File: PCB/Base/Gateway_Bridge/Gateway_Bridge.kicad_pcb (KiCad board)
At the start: 2 copper layers, 98.9 x 70.1 mm, 58 parts, among them J1 J_DIAG, J2 J_I2C2, J3 STM32_Breakout, J5 J_CAN_TERM, J6 J_I2C1, J7 J_SWD, J8 J_BUS_IN, J9 J_BUS_OUT, SW1 RESET, U1 STM32F103C8Tx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

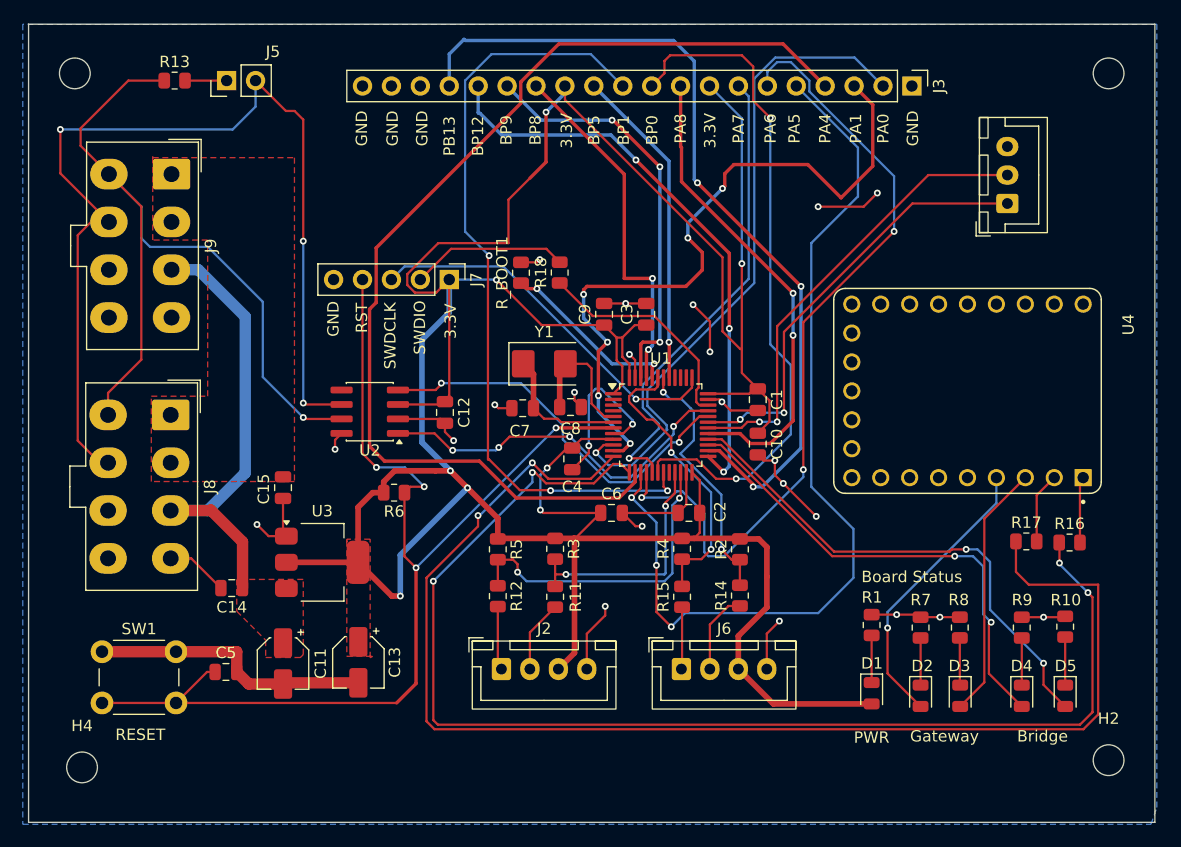
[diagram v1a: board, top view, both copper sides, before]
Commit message: feat(pcb): bus power distribution — poured rails, solid bus pads, GND stitching (base boards)
PanelGroup_Base + Gateway/Bridge: +12V/+5V/GND poured (12V top, 5V bottom,
GND both layers), solid pad connection on J_BUS power+GND pins (CAN default),
GND stitching vias. Sized for per-console injection (5A/12V, 2A/5V); copper
poured so the connector (8-9A/pin) is the limit, not traces.
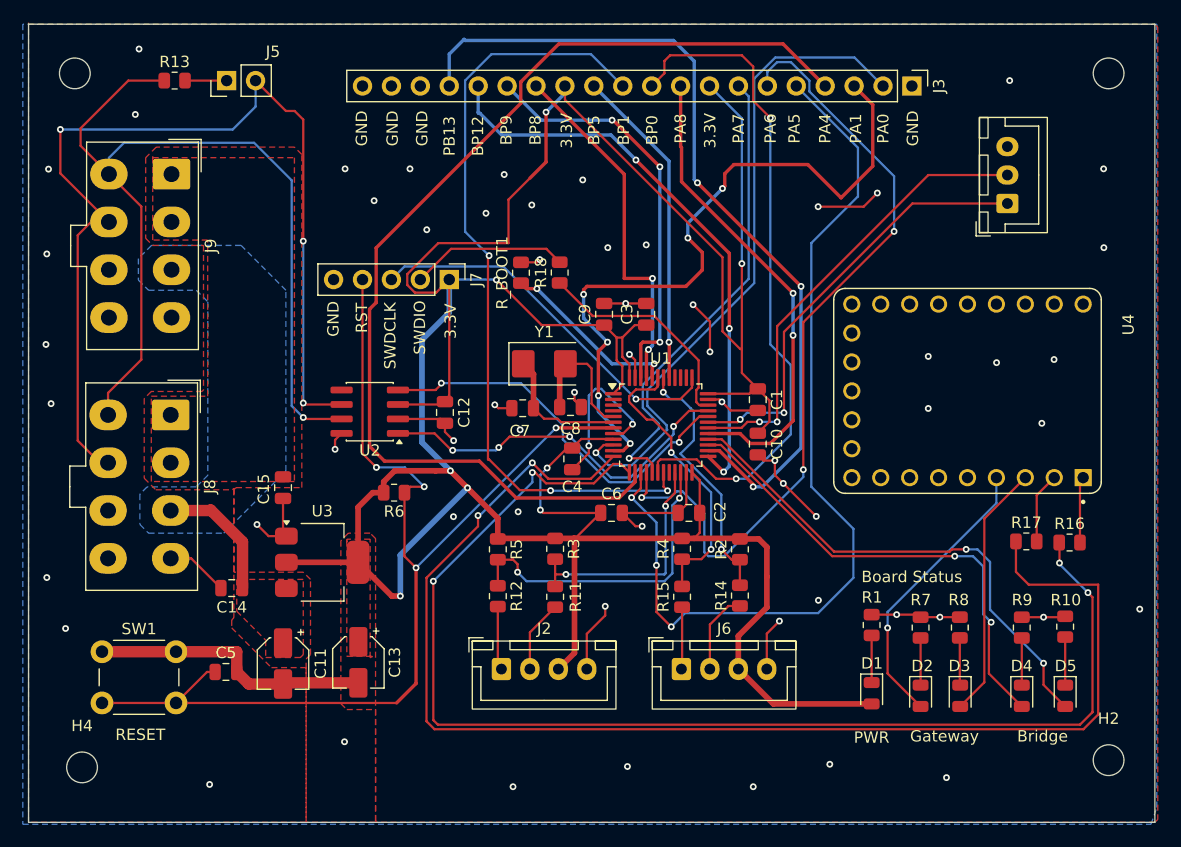
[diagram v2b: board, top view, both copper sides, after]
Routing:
- net +5V: track 41.4 -> 11.6 mm
- net /CANH: track 72.5 -> 81.7 mm
- net GND: vias 24 -> 62
- added copper zone on B.Cu, net +5V
- added copper zone on F.Cu, net GND
